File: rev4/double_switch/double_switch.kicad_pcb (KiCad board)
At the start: 2 copper layers, 17.1 x 39.4 mm, 5 parts, among them J1 Conn_01x03, SW1 SW_Push_45deg, SW2 SW_Push_45deg

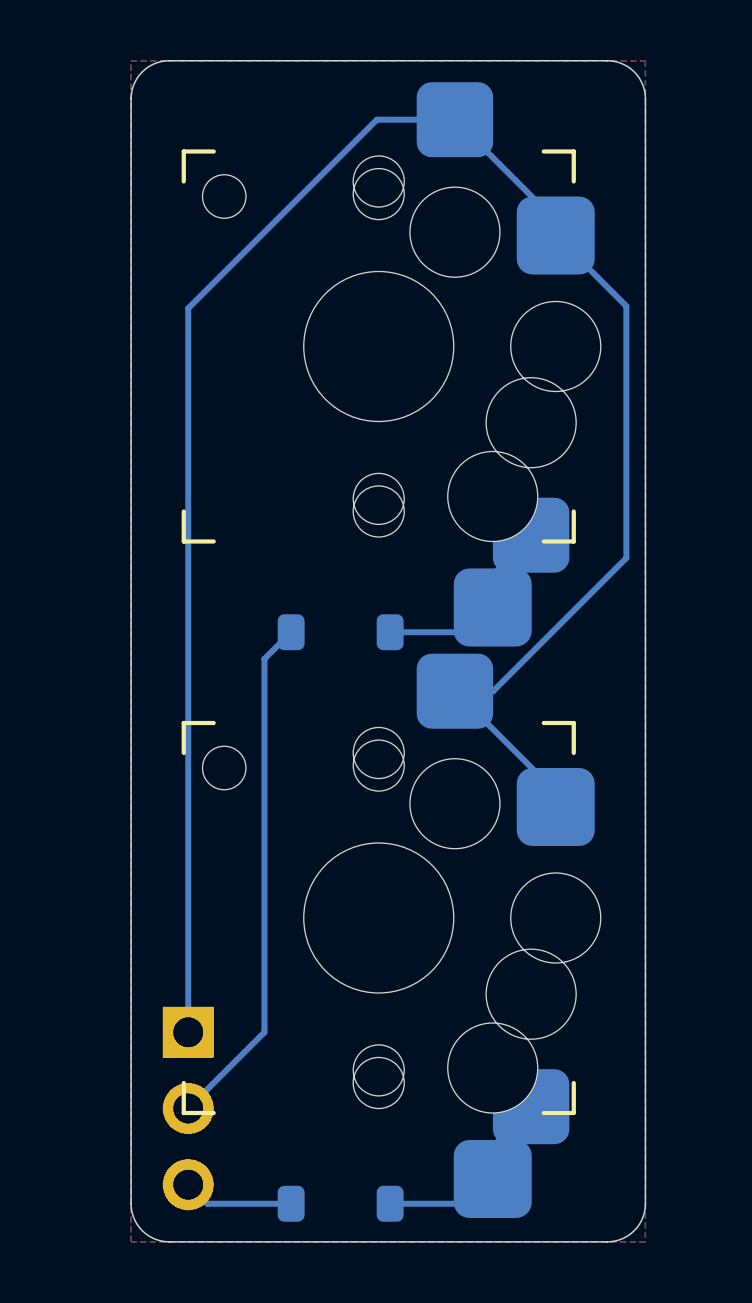
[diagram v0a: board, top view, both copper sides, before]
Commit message: feat: reduce Y length
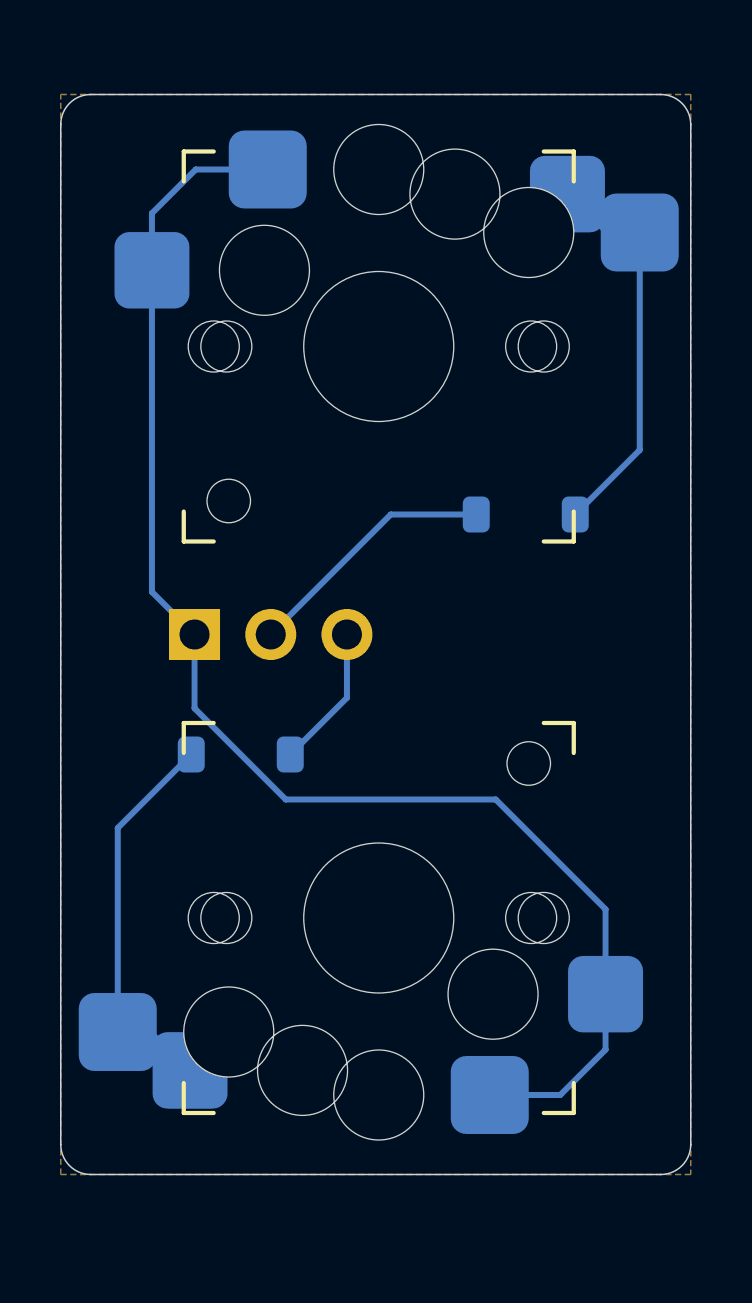
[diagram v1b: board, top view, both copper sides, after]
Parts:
- moved D2 15.3 mm to (160.5, 102.5), turned to 180 degrees
- moved J1 13.3 mm to (159.0, 98.5), turned to -90 degrees
- moved D1 7.31 mm to (170.0, 94.5)
- turned SW1 to 180 degrees
- turned SW2 to 0 degrees
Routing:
- net COL0: track 65.4 -> 47.2 mm
- net ROW0: track 17.3 -> 8.51 mm
- net Net-(D1-A): track 6.69 -> 13.2 mm
- net Net-(D2-A): track 6.69 -> 13.2 mm
- net ROW1: track 3.69 -> 4.78 mm
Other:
- board size 17.1 x 39.4 mm -> 21 x 36 mm

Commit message: feat: update double switch layout
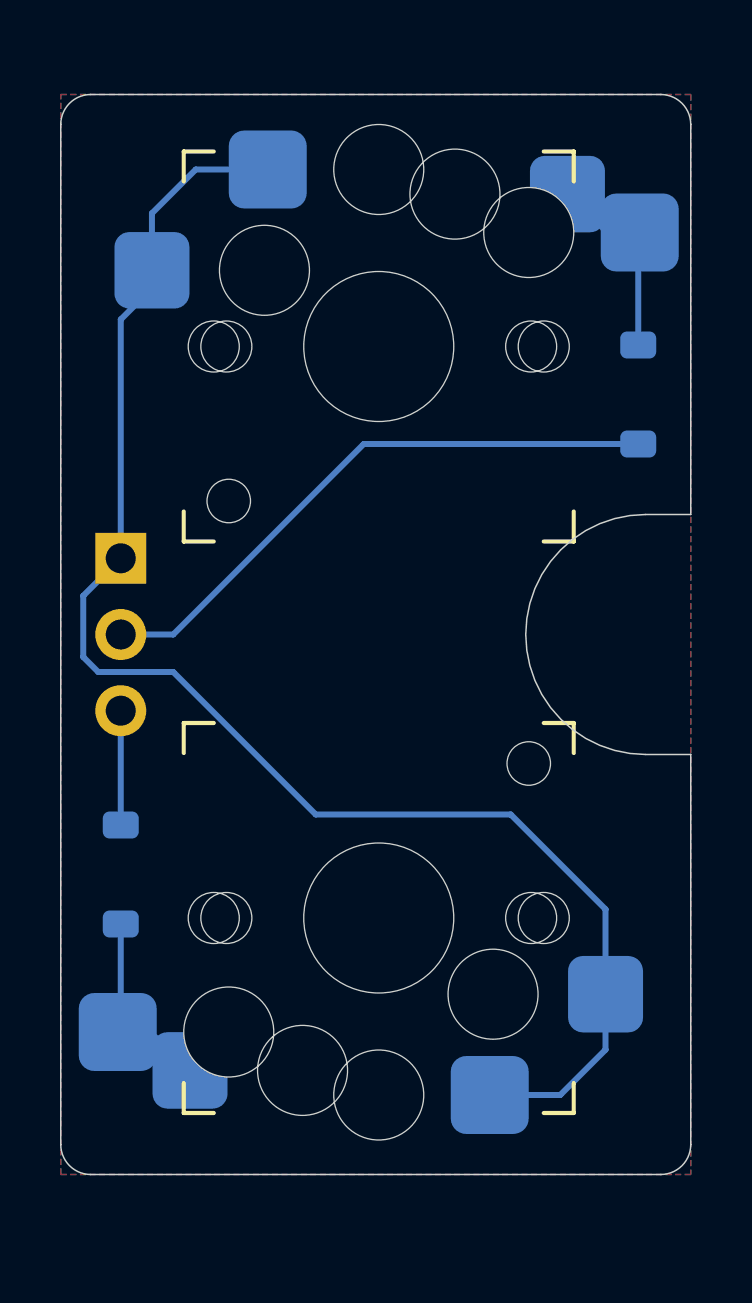
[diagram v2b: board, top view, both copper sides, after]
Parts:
- moved D2 5.66 mm to (156.5, 106.5), turned to -90 degrees
- moved D1 5.48 mm to (173.8, 90.5), turned to 90 degrees
- moved J1 3.54 mm to (156.5, 96.0), turned to 180 degrees
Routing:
- net ROW0: track 8.51 -> 19.9 mm
- net Net-(D2-A): track 13.2 -> 6.57 mm
- net Net-(D1-A): track 13.2 -> 6.70 mm
- net COL0: track 47.2 -> 50.3 mm
- net ROW1: track 4.78 -> 3.81 mm
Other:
- outline, holes or cut-outs redrawn
